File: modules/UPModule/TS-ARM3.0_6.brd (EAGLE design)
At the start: 42.3 x 27.4 mm, 82 parts, among them IC1 LPC1115, IC100 BD9G101, P1 , P10 , P11 , P12 , P13 , P14 , P2 , P3 , P4 , P5 , P6 , P7 , P8 , P9 , Q1 FA-20H, T1 BC856, T2 BCP52, T3 BC847, X1 EIB

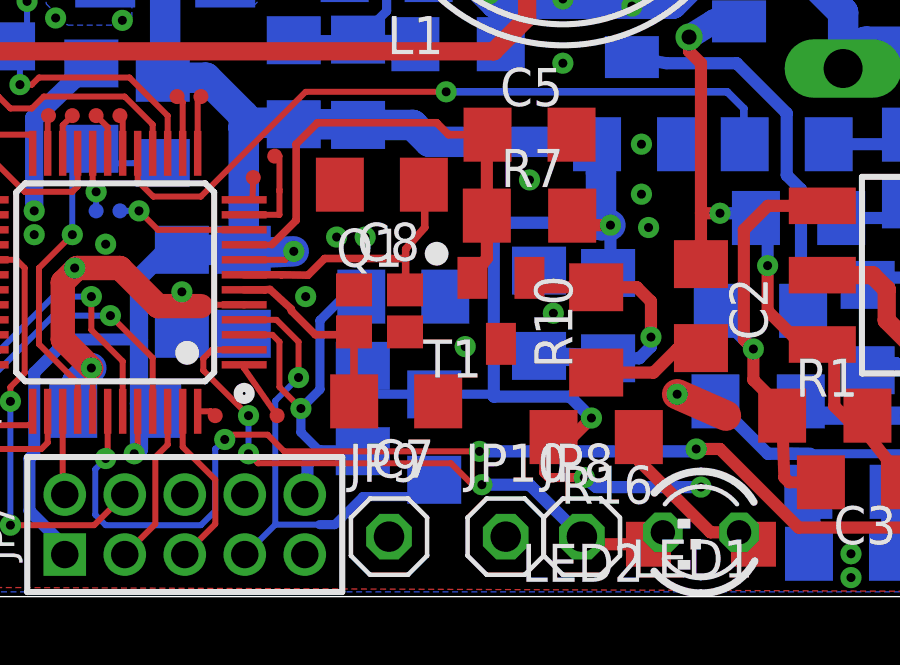
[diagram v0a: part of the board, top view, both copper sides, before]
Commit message: Quarz footprint auf ASF geändert
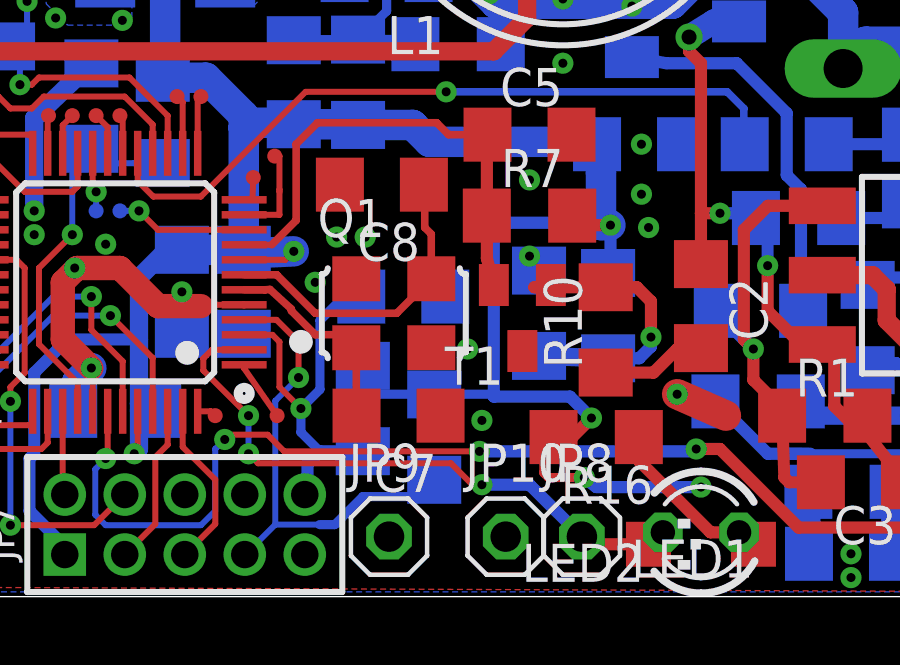
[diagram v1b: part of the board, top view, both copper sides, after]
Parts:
- Q1: value FA-20H -> FA-ASF; device crystal:FA-20H -> crystal:ASF
- moved T1 0.75 mm to (24.7, 9.29)
- moved Q1 0.48 mm to (20.4, 9.45)
- moved C7 0.48 mm to (20.6, 6.03)
- moved R10 0.32 mm to (27.5, 8.89)
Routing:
- net N$5: track 9.38 -> 10.5 mm
- net N$14: track 10.2 -> 10.7 mm
- net GND: vias 45 -> 46
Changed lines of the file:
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@@
 <layer number="39" name="tKeepout" color="4" fill="11" visible="no" active="yes"/>
 <layer number="40" name="bKeepout" color="1" fill="11" visible="no" active="yes"/>
-<layer number="41" name="tRestrict" color="4" fill="10" visible="no" active="yes"/>
+<layer number="41" name="tRestrict" color="4" fill="10" visible="yes" active="yes"/>
 <layer number="42" name="bRestrict" color="1" fill="10" visible="no" active="yes"/>
 <layer number="43" name="vRestrict" color="2" fill="10" visible="no" active="yes"/>
@@
 <layer number="49" name="Reference" color="7" fill="1" visible="no" active="yes"/>
 <layer number="50" name="dxf" color="7" fill="1" visible="no" active="no"/>
-<layer number="51" name="tDocu" color="7" fill="1" visible="no" active="yes"/>
+<layer number="51" name="tDocu" color="7" fill="1" visible="yes" active="yes"/>
 <layer number="52" name="bDocu" color="7" fill="1" visible="no" active="yes"/>
 <layer number="53" name="tGND_GNDA" color="7" fill="9" visible="no" active="no"/>
@@
 <text x="39.84625" y="16.35125" size="1.778" layer="21">-</text>
 <rectangle x1="1.825625" y1="1.666875" x2="40.825625" y2="25.806875" layer="248"/>
-<circle x="21.828125" y="11.43" radius="0.396875" width="0" layer="21"/>
+<circle x="17.30375" y="8.493125" radius="0.396875" width="0" layer="21"/>
 </plain>
 <attributes>
@@
 <attribute name="VALUE" x="33.258125" y="6.985" size="1.27" layer="28" rot="MR0"/>
 </element>
-<element name="R10" library="rcl" package="R1206" value="10k" x="27.14625" y="8.89" smashed="yes" rot="R90">
-<attribute name="REICHELT" value="SMD-0805 10,0K" x="27.14625" y="8.89" size="1.778" layer="27" rot="R90" display="off"/>
-<attribute name="NAME" x="26.3525" y="7.62" size="1.27" layer="25" rot="R90"/>
-<attribute name="VALUE" x="29.68625" y="8.255" size="1.27" layer="27" rot="R90"/>
+<element name="R10" library="rcl" package="R1206" value="10k" x="27.46375" y="8.89" smashed="yes" rot="R90">
+<attribute name="REICHELT" value="SMD-0805 10,0K" x="27.46375" y="8.89" size="1.778" layer="27" rot="R90" display="off"/>
+<attribute name="NAME" x="26.67" y="7.62" size="1.27" layer="25" rot="R90"/>
+<attribute name="VALUE" x="30.00375" y="8.255" size="1.27" layer="27" rot="R90"/>
 </element>
 <element name="C9" library="rcl" package="C1206" value="10n" x="20.716875" y="10.00125" smashed="yes" rot="MR0">
@@
 <attribute name="VALUE" x="36.4617" y="13.255625" size="1.27" layer="27" rot="R270"/>
 </element>
-<element name="T1" library="transistor-pnp" package="SOT23-BEC" value="BC856" x="23.97125" y="9.525" smashed="yes" rot="R180">
-<attribute name="REICHELT" value="BC 856B SMD" x="23.97125" y="9.525" size="1.778" layer="27" rot="R180" display="off"/>
-<attribute name="NAME" x="23.33625" y="8.5725" size="1.27" layer="25" rot="R180"/>
-<attribute name="VALUE" x="25.87625" y="12.7" size="1.27" layer="27" rot="R180"/>
+<element name="T1" library="transistor-pnp" package="SOT23-BEC" value="BC856" x="24.685625" y="9.286875" smashed="yes" rot="R180">
+<attribute name="REICHELT" value="BC 856B SMD" x="24.685625" y="9.286875" size="1.778" layer="27" rot="R180" display="off"/>
+<attribute name="NAME" x="24.050625" y="8.334375" size="1.27" layer="25" rot="R180"/>
+<attribute name="VALUE" x="26.590625" y="12.461875" size="1.27" layer="27" rot="R180"/>
 </element>
 <element name="C13" library="rcl" package="C1206" value="100n" x="11.1125" y="6.19125" smashed="yes" rot="MR180">
@@
 <attribute name="REICHELT" value="SMD-LED 0805 RT" x="30.63875" y="2.143125" size="1.778" layer="27" rot="R180" display="off"/>
 </element>
-<element name="C7" library="rcl" package="C1206" value="10n" x="20.47875" y="6.50875" rot="R180"/>
+<element name="C7" library="rcl" package="C1206" value="10n" x="20.558125" y="6.0325" rot="R180"/>
 <element name="JP10" library="pinhead" package="1X01" value="" x="24.13" y="2"/>
-<element name="Q1" library="crystal" package="FA-20H" value="FA-20H" x="19.923125" y="9.525"/>
+<element name="Q1" library="crystal" package="ASF" value="FA-ASF" x="20.399375" y="9.445625"/>
 <element name="C8" library="rcl" package="C1206" value="10n" x="20.0025" y="13.731875" rot="R180"/>
 </elements>
@@
 <wire x1="29.845" y1="6.746875" x2="31.4706" y2="6.0325" width="1.016" layer="1"/>
 <via x="29.845" y="6.746875" extent="1-16" drill="0.3"/>
-<via x="22.780625" y="8.334375" extent="1-16" drill="0.3"/>
+<via x="23.33625" y="5.87375" extent="1-16" drill="0.3"/>
 <wire x1="17.4325" y1="1.4025" x2="17.43625" y2="1.4025" width="1.016" layer="1"/>
 <wire x1="17.43625" y1="1.4025" x2="17.4625" y2="1.42875" width="1.016" layer="1"/>
@@
 <via x="37.861875" y="11.58875" extent="1-16" drill="0.3"/>
 <via x="38.814375" y="13.17625" extent="1-16" drill="0.3"/>
-<via x="25.7175" y="9.445625" extent="1-16" drill="0.3"/>
+<via x="24.92375" y="11.350625" extent="1-16" drill="0.3"/>
 <via x="38.338125" y="5.3975" extent="1-16" drill="0.3"/>
 <wire x1="34.217375" y1="3.4925" x2="34.217375" y2="1.45075" width="0.8128" layer="16"/>
@@
 <contactref element="Q1" pad="2"/>
 <contactref element="Q1" pad="4"/>
-<via x="17.4625" y="10.00125" extent="1-16" drill="0.3"/>
+<via x="17.78" y="10.4775" extent="1-16" drill="0.3"/>
+<via x="22.86" y="8.255" extent="1-16" drill="0.3"/>
 </signal>
 <signal name="LX">
@@
 <wire x1="23.50175" y1="14.836375" x2="23.495" y2="14.843125" width="0.2" layer="1"/>
 <wire x1="23.50175" y1="12.7" x2="23.502" y2="11.278" width="0.4064" layer="1"/>
-<wire x1="23.502" y1="11.278" x2="23.02125" y2="10.625" width="0.4064" layer="1"/>
+<wire x1="23.502" y1="11.278" x2="23.735625" y2="10.386875" width="0.4064" layer="1"/>
 <wire x1="16.33125" y1="11.7275" x2="17.145" y2="12.54125" width="0.254" layer="1"/>
 <wire x1="17.145" y1="12.54125" x2="17.145" y2="15.08125" width="0.254" layer="1"/>
@@
 <contactref element="C2" pad="2"/>
 <wire x1="31.1125" y1="7.62" x2="30.63875" y2="8.28375" width="0.2" layer="1"/>
-<wire x1="27.14625" y1="7.468" x2="29.058" y2="7.468" width="0.4064" layer="1"/>
+<wire x1="27.46375" y1="7.468" x2="29.058" y2="7.468" width="0.4064" layer="1"/>
 <wire x1="29.058" y1="7.468" x2="29.845" y2="8.255" width="0.4064" layer="1"/>
 <wire x1="29.845" y1="8.255" x2="30.61" y2="8.255" width="0.4064" layer="1"/>
@@
 <contactref element="T1" pad="B"/>
 <via x="28.971875" y="8.651875" extent="1-16" drill="0.3"/>
-<wire x1="26.82425" y1="10.14875" x2="27.14625" y2="10.312" width="0.4064" layer="1"/>
-<wire x1="27.14625" y1="10.312" x2="28.502375" y2="10.312" width="0.4064" layer="1"/>
+<wire x1="26.82425" y1="10.14875" x2="27.46375" y2="10.312" width="0.4064" layer="1"/>
+<wire x1="27.46375" y1="10.312" x2="28.502375" y2="10.312" width="0.4064" layer="1"/>
 <wire x1="28.502375" y1="10.312" x2="28.971875" y2="9.8425" width="0.4064" layer="1"/>
 <wire x1="28.971875" y1="9.8425" x2="28.971875" y2="8.651875" width="0.4064" layer="1"/>
-<wire x1="24.92125" y1="10.625" x2="25.0845" y2="10.312" width="0.4064" layer="1"/>
-<wire x1="25.0845" y1="10.312" x2="27.14625" y2="10.312" width="0.4064" layer="1"/>
+<wire x1="25.635625" y1="10.386875" x2="25.0845" y2="10.312" width="0.4064" layer="1"/>
+<wire x1="25.0845" y1="10.312" x2="27.46375" y2="10.312" width="0.4064" layer="1"/>
 <wire x1="27.543125" y1="7.94425" x2="28.58175" y2="7.94425" width="0.4064" layer="16"/>
 <wire x1="28.58175" y1="7.94425" x2="28.971875" y2="8.334375" width="0.4064" layer="16"/>
@@
 <wire x1="16.98625" y1="9.525" x2="17.78" y2="8.73125" width="0.254" layer="1"/>
 <wire x1="17.78" y1="8.73125" x2="18.9" y2="8.73125" width="0.254" layer="1"/>
-<wire x1="18.9" y1="8.73125" x2="19.073125" y2="8.825" width="0.254" layer="1"/>
+<wire x1="18.9" y1="8.73125" x2="19.149375" y2="8.295625" width="0.254" layer="1"/>
 <contactref element="C7" pad="2"/>
-<wire x1="19.073125" y1="8.825" x2="19.073125" y2="6.42375" width="0.254" layer="1"/>
-<wire x1="19.073125" y1="6.42375" x2="19.07875" y2="6.50875" width="0.254" layer="1"/>
+<wire x1="19.149375" y1="8.295625" x2="19.1525" y2="6.42375" width="0.254" layer="1"/>
+<wire x1="19.1525" y1="6.42375" x2="19.158125" y2="6.0325" width="0.254" layer="1"/>
 </signal>
 <signal name="N$5">
 <contactref element="IC1" pad="7"/>
 <contactref element="Q1" pad="3"/>
-<wire x1="15.4125" y1="10.7275" x2="16.656875" y2="10.7275" width="0.254" layer="1"/>
-<wire x1="16.656875" y1="10.7275" x2="17.541875" y2="10.715625" width="0.254" layer="1"/>
-<wire x1="17.541875" y1="10.715625" x2="18.0975" y2="11.27125" width="0.254" layer="1"/>
-<wire x1="18.0975" y1="11.27125" x2="20.79625" y2="11.27125" width="0.254" layer="1"/>
-<wire x1="20.79625" y1="11.27125" x2="20.79625" y2="10.248125" width="0.254" layer="1"/>
-<wire x1="20.79625" y1="10.248125" x2="20.773125" y2="10.225" width="0.254" layer="1"/>
 <contactref element="C8" pad="1"/>
-<wire x1="20.79625" y1="11.27125" x2="20.79625" y2="11.58875" width="0.254" layer="1"/>
-<wire x1="20.79625" y1="11.58875" x2="21.43125" y2="12.303125" width="0.254" layer="1"/>
 <wire x1="21.43125" y1="12.303125" x2="21.43125" y2="13.703125" width="0.254" layer="1"/>
 <wire x1="21.43125" y1="13.703125" x2="21.4025" y2="13.731875" width="0.254" layer="1"/>
+<wire x1="17.78" y1="9.445625" x2="20.499375" y2="9.445625" width="0.254" layer="1"/>
+<wire x1="20.499375" y1="9.445625" x2="21.649375" y2="10.595625" width="0.254" layer="1"/>
+<wire x1="15.4125" y1="10.7275" x2="16.498125" y2="10.7275" width="0.254" layer="1"/>
+<wire x1="16.498125" y1="10.7275" x2="17.78" y2="9.445625" width="0.254" layer="1"/>
+<wire x1="21.649375" y1="10.595625" x2="21.649375" y2="12.085" width="0.254" layer="1"/>
+<wire x1="21.649375" y1="12.085" x2="21.43125" y2="12.303125" width="0.254" layer="1"/>
 </signal>
 </signals>

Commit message: drc debug
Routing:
- net N$14: track 10.7 -> 9.61 mm
- net GND: vias 46 -> 45
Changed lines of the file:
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@@
 <layer number="17" name="Pads" color="2" fill="1" visible="yes" active="yes"/>
 <layer number="18" name="Vias" color="2" fill="1" visible="yes" active="yes"/>
-<layer number="19" name="Unrouted" color="6" fill="1" visible="yes" active="yes"/>
+<layer number="19" name="Unrouted" color="6" fill="1" visible="no" active="yes"/>
 <layer number="20" name="Dimension" color="15" fill="1" visible="yes" active="yes"/>
-<layer number="21" name="tPlace" color="7" fill="1" visible="yes" active="yes"/>
+<layer number="21" name="tPlace" color="7" fill="1" visible="no" active="yes"/>
 <layer number="22" name="bPlace" color="7" fill="1" visible="yes" active="yes"/>
-<layer number="23" name="tOrigins" color="15" fill="1" visible="yes" active="yes"/>
+<layer number="23" name="tOrigins" color="15" fill="1" visible="no" active="yes"/>
 <layer number="24" name="bOrigins" color="15" fill="1" visible="yes" active="yes"/>
 <layer number="25" name="tNames" color="7" fill="1" visible="no" active="yes"/>
@@
 <layer number="39" name="tKeepout" color="4" fill="11" visible="no" active="yes"/>
 <layer number="40" name="bKeepout" color="1" fill="11" visible="no" active="yes"/>
-<layer number="41" name="tRestrict" color="4" fill="10" visible="yes" active="yes"/>
+<layer number="41" name="tRestrict" color="4" fill="10" visible="no" active="yes"/>
 <layer number="42" name="bRestrict" color="1" fill="10" visible="no" active="yes"/>
 <layer number="43" name="vRestrict" color="2" fill="10" visible="no" active="yes"/>
@@
 <layer number="49" name="Reference" color="7" fill="1" visible="no" active="yes"/>
 <layer number="50" name="dxf" color="7" fill="1" visible="no" active="no"/>
-<layer number="51" name="tDocu" color="7" fill="1" visible="yes" active="yes"/>
+<layer number="51" name="tDocu" color="7" fill="1" visible="no" active="yes"/>
 <layer number="52" name="bDocu" color="7" fill="1" visible="no" active="yes"/>
 <layer number="53" name="tGND_GNDA" color="7" fill="9" visible="no" active="no"/>
@@
 <attribute name="REICHELT" value="X7R-G0805 100N" x="6.50875" y="22.463125" size="1.778" layer="27" rot="R90" display="off"/>
 <attribute name="NAME" x="5.715" y="21.034375" size="1.27" layer="25" rot="R90"/>
-<attribute name="VALUE" x="8.5725" y="21.193125" size="1.27" layer="27" rot="R90"/>
+<attribute name="VALUE" x="8.969375" y="20.6375" size="1.27" layer="27" rot="R90"/>
 </element>
 <element name="IC100" library="Stefan_selfbus" package="SOT23-6" value="BD9G101" x="19.52625" y="23.495" smashed="yes" rot="MR270">
@@
 <attribute name="REICHELT" value="VF 100/35 K-D8" x="14.2875" y="23.8125" size="1.778" layer="27" display="off"/>
 <attribute name="NAME" x="11.1125" y="27.6225" size="1.27" layer="25"/>
-<attribute name="VALUE" x="6.35" y="19.05" size="1.27" layer="27"/>
+<attribute name="VALUE" x="10.95375" y="25.24125" size="1.27" layer="27"/>
 </element>
 <element name="R4" library="rcl" package="R1206" value="2k2" x="36.195" y="8.969375" smashed="yes" rot="MR270">
@@
 <attribute name="REICHELT" value="L-11P 150M" x="26.035" y="24.526875" size="1.778" layer="27" rot="R180" display="off"/>
 <attribute name="NAME" x="22.054" y="19.351875" size="1.27" layer="25" rot="R180"/>
-<attribute name="VALUE" x="29.285" y="27.526875" size="1.27" layer="27" rot="R180"/>
+<attribute name="VALUE" x="29.999375" y="22.446875" size="1.27" layer="27" rot="R180"/>
 </element>
 <element name="R3" library="rcl" package="R1206" value="1k" x="32.623125" y="9.525" smashed="yes" rot="MR0">
@@
 <attribute name="REICHELT" value="X7R-G0805 10N" x="36.03625" y="3.81" size="1.778" layer="27" rot="R180" display="off"/>
 <attribute name="NAME" x="37.1475" y="3.01625" size="1.27" layer="25" rot="R180"/>
-<attribute name="VALUE" x="37.30625" y="6.35" size="1.27" layer="27" rot="R180"/>
+<attribute name="VALUE" x="39.52875" y="1.5875" size="1.27" layer="27" rot="R180"/>
 </element>
 <element name="R1" library="rcl" package="R1206" value="1k" x="34.76625" y="6.0325" smashed="yes" rot="R180">
 <attribute name="REICHELT" value="SMD-0805 1,00K" x="34.76625" y="6.0325" size="1.778" layer="27" rot="R180" display="off"/>
 <attribute name="NAME" x="35.8775" y="7.9375" size="1.27" layer="25" rot="R180"/>
-<attribute name="VALUE" x="35.40125" y="8.5725" size="1.27" layer="27" rot="R180"/>
+<attribute name="VALUE" x="38.25875" y="8.175625" size="1.27" layer="27" rot="R180"/>
 </element>
 <element name="R2" library="rcl" package="R1206" value="5R6" x="32.54375" y="6.50875" smashed="yes" rot="MR180">
@@
 <attribute name="REICHELT" value="SMD-0805 10,0K" x="24.92375" y="12.7" size="1.778" layer="27" display="off"/>
 <attribute name="NAME" x="23.97125" y="13.6525" size="1.27" layer="25"/>
-<attribute name="VALUE" x="24.28875" y="10.16" size="1.27" layer="27"/>
+<attribute name="VALUE" x="27.46375" y="13.335" size="1.27" layer="27"/>
 </element>
 <element name="D3" library="diode" package="MINIMELF" value="1N4148" x="33.575625" y="26.035" smashed="yes" rot="MR180">
@@
 <attribute name="REICHELT" value="NPO-G0805 100P" x="24.92375" y="15.39875" size="1.778" layer="27" rot="R180" display="off"/>
 <attribute name="NAME" x="26.035" y="17.62125" size="1.27" layer="25" rot="R180"/>
-<attribute name="VALUE" x="26.19375" y="17.93875" size="1.27" layer="27" rot="R180"/>
+<attribute name="VALUE" x="26.67" y="18.176875" size="1.27" layer="27" rot="R180"/>
 </element>
 <element name="R14" library="rcl" package="R1206" value="100k" x="19.3675" y="6.270625" smashed="yes" rot="MR90">
@@
 <attribute name="REICHELT" value="BCP 52-16 SMD" x="37.7825" y="10.715625" size="1.778" layer="27" rot="R270" display="off"/>
 <attribute name="NAME" x="40.0558" y="7.540625" size="1.27" layer="25" rot="R270"/>
-<attribute name="VALUE" x="36.4617" y="13.255625" size="1.27" layer="27" rot="R270"/>
+<attribute name="VALUE" x="36.30295" y="13.17625" size="1.27" layer="27" rot="R270"/>
 </element>
 <element name="T1" library="transistor-pnp" package="SOT23-BEC" value="BC856" x="24.685625" y="9.286875" smashed="yes" rot="R180">
 <attribute name="REICHELT" value="BC 856B SMD" x="24.685625" y="9.286875" size="1.778" layer="27" rot="R180" display="off"/>
 <attribute name="NAME" x="24.050625" y="8.334375" size="1.27" layer="25" rot="R180"/>
-<attribute name="VALUE" x="26.590625" y="12.461875" size="1.27" layer="27" rot="R180"/>
+<attribute name="VALUE" x="28.019375" y="7.064375" size="1.27" layer="27" rot="R180"/>
 </element>
 <element name="C13" library="rcl" package="C1206" value="100n" x="11.1125" y="6.19125" smashed="yes" rot="MR180">
@@
 <attribute name="REICHELT" value="SMD ZF 3,6" x="40.9575" y="5.08" size="1.778" layer="27" rot="R90" display="off"/>
 <attribute name="NAME" x="39.8145" y="4.3815" size="1.27" layer="25" rot="R90"/>
-<attribute name="VALUE" x="43.3705" y="3.429" size="1.27" layer="27" rot="R90"/>
+<attribute name="VALUE" x="39.798625" y="3.984625" size="1.27" layer="27" rot="R90"/>
 </element>
 <element name="C10" library="rcl" package="C1206" value="100n" x="35.639375" y="1.42875" smashed="yes" rot="MR180">
@@
 <attribute name="REICHELT" value="SMD-LED 0805 RT" x="30.63875" y="1.74625" size="1.778" layer="27" rot="R90" display="off"/>
 <attribute name="NAME" x="32.385" y="1.905" size="1.27" layer="25" rot="R180"/>
-<attribute name="VALUE" x="31.90875" y="4.28625" size="1.27" layer="27" rot="R180"/>
+<attribute name="VALUE" x="31.988125" y="1.508125" size="1.27" layer="27" rot="R180"/>
 </element>
 <element name="R16" library="rcl" package="R1206" value="1k" x="27.14625" y="5.318125" smashed="yes" rot="R180">
 <attribute name="REICHELT" value="SMD-0805 1,00K" x="27.14625" y="5.318125" size="1.778" layer="27" rot="R180" display="off"/>
 <attribute name="NAME" x="29.05125" y="4.365625" size="1.27" layer="25" rot="R180"/>
-<attribute name="VALUE" x="27.78125" y="7.858125" size="1.27" layer="27" rot="R180"/>
+<attribute name="VALUE" x="25.955625" y="4.048125" size="1.27" layer="27" rot="R180"/>
 </element>
 <element name="JP1" library="selfbus" package="SMD1,27X2,54X8" value="WIREPADX8" x="2.2225" y="10.795"/>
@@
 <via x="37.861875" y="11.58875" extent="1-16" drill="0.3"/>
 <via x="38.814375" y="13.17625" extent="1-16" drill="0.3"/>
-<via x="24.92375" y="11.350625" extent="1-16" drill="0.3"/>
 <via x="38.338125" y="5.3975" extent="1-16" drill="0.3"/>
 <wire x1="34.217375" y1="3.4925" x2="34.217375" y2="1.45075" width="0.8128" layer="16"/>
@@
 <wire x1="28.502375" y1="10.312" x2="28.971875" y2="9.8425" width="0.4064" layer="1"/>
 <wire x1="28.971875" y1="9.8425" x2="28.971875" y2="8.651875" width="0.4064" layer="1"/>
-<wire x1="25.635625" y1="10.386875" x2="25.0845" y2="10.312" width="0.4064" layer="1"/>
-<wire x1="25.0845" y1="10.312" x2="27.46375" y2="10.312" width="0.4064" layer="1"/>
+<wire x1="25.635625" y1="10.386875" x2="25.798875" y2="10.312" width="0.4064" layer="1"/>
 <wire x1="27.543125" y1="7.94425" x2="28.58175" y2="7.94425" width="0.4064" layer="16"/>
 <wire x1="28.58175" y1="7.94425" x2="28.971875" y2="8.334375" width="0.4064" layer="16"/>
 <wire x1="28.971875" y1="8.334375" x2="28.971875" y2="8.651875" width="0.4064" layer="16"/>
 <wire x1="25.24125" y1="8.023625" x2="27.543125" y2="7.94425" width="0.6096" layer="16"/>
+<wire x1="25.798875" y1="10.312" x2="27.46375" y2="10.312" width="0.4064" layer="1"/>
 </signal>
 <signal name="N$9">
